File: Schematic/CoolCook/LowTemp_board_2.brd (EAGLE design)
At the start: 100 x 69.8 mm, 11 parts, among them SW2 EC11B-V

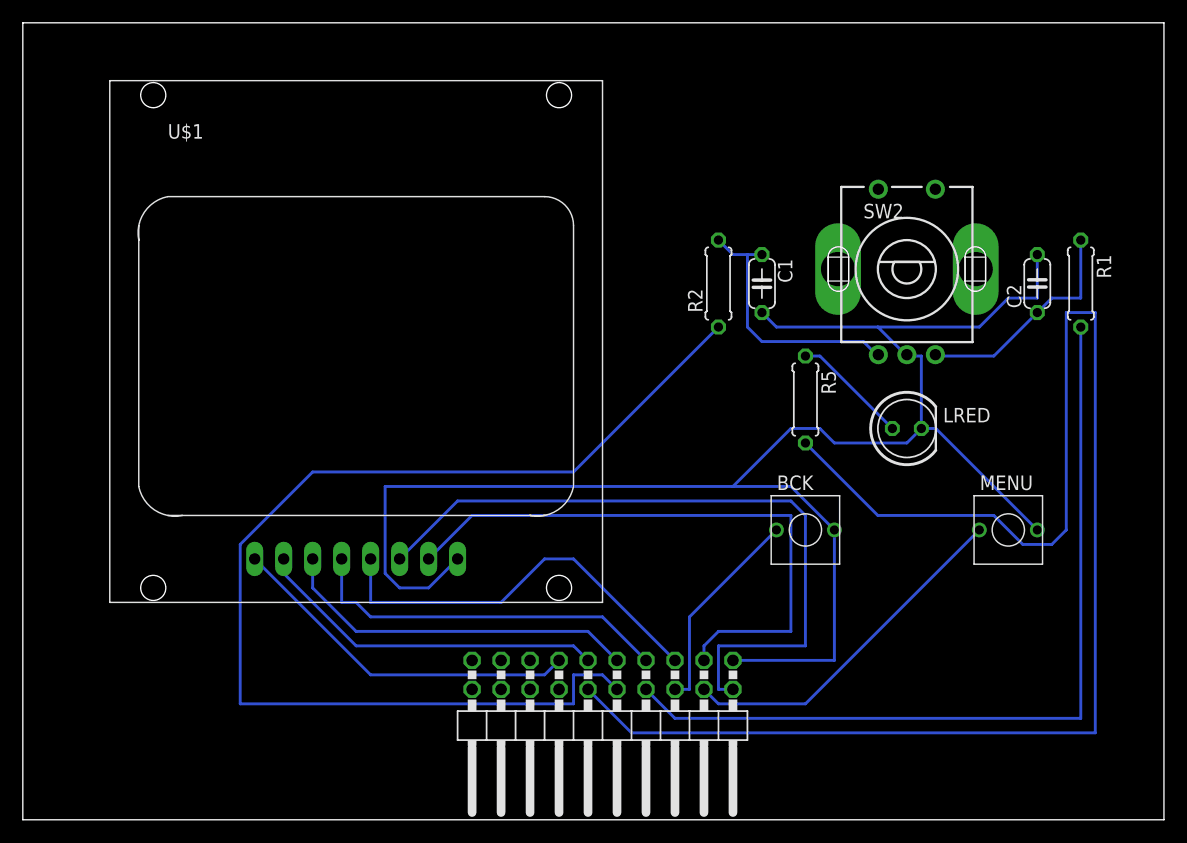
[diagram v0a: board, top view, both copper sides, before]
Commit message: Update schematic in two boards (test and work great) Reverse rotation in arduino program
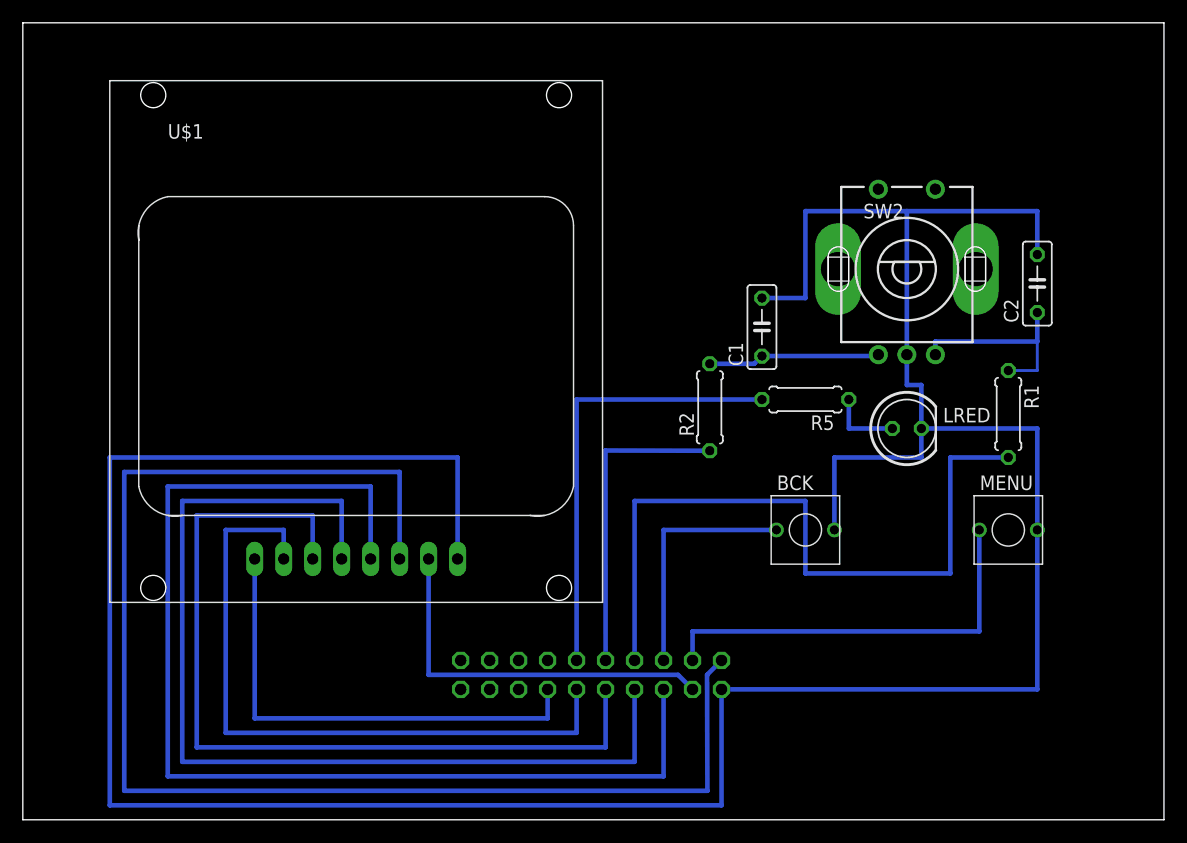
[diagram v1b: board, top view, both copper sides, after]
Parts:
- C1, C2: device rcl:C050-024X044 -> rcl:C050-025X075
- moved R1 13.1 mm to (86.4, 35.6)
- moved R2 10.9 mm to (60.2, 36.1)
- moved U$2 7.69 mm to (49.8, 16.5), flipped to the bottom, turned to 0 degrees
- moved C1 3.81 mm to (64.8, 43.2), turned to 90 degrees
- turned R5 to 180 degrees
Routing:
- net AGND: track 151.2 -> 266.7 mm
- net HEAT: track 131.5 -> 39.1 mm
- net ROT1: track 99.9 -> 27.5 mm
- net SCLK: track 35.7 -> 100.6 mm
- net +3V3: track 62.3 -> 122.7 mm
- net SDIN: track 32.6 -> 87.9 mm
- net SDC: track 31.8 -> 75.2 mm
- net SCE: track 31.1 -> 60.0 mm
- net SBL: track 52.9 -> 33.8 mm
- net SRST: track 31.4 -> 42.2 mm
- net ROT2: track 73.4 -> 63.2 mm
- net N$1: track 23.3 -> 15.1 mm
- net BTMENU: track 31.0 -> 36.6 mm
- net N$4: track 10.3 -> 6.35 mm
- net BTBCK: track 18.4 -> 21.3 mm
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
